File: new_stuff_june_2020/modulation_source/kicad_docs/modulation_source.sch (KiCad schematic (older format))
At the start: 72 parts, among them J1 power_in, Q1 BC560, Q2 BC560, Q3 BF245A, Q4 BC550, Q5 BC550, Q6 BC550, U1 LM13700, U2 TL072, U3 TL072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

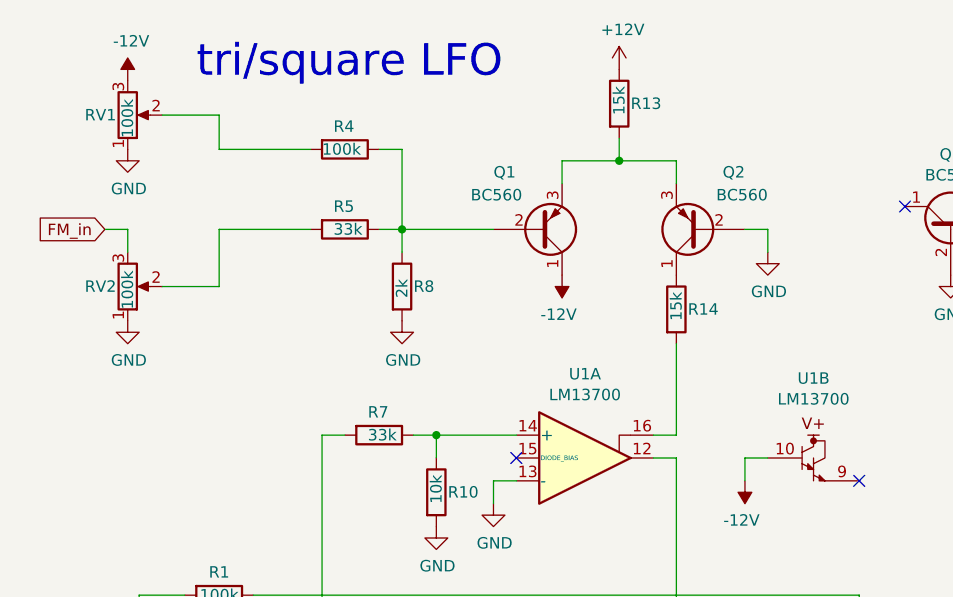
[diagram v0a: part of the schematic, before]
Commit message: change modulation-source fm circuit, make new gerbers
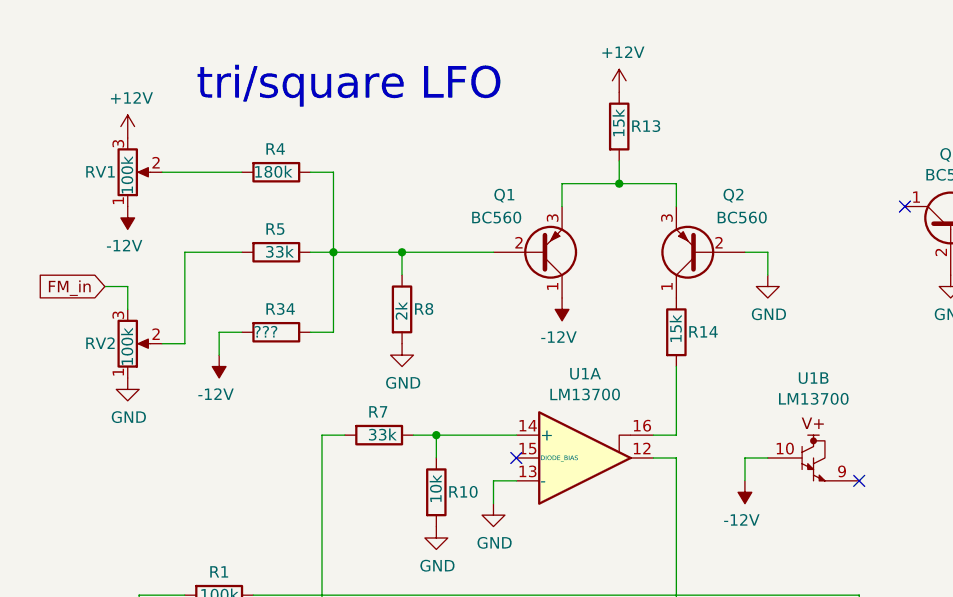
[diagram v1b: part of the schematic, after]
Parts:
- added R34: ???, Resistor_SMD:R_0805_2012Metric_Pad1.15x1.40mm_HandSolder, symbol Device:R
- R4: value 100k -> 180k
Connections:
- net +12V: now also RV1.3
- net -12V: now also RV1.1, R34.2; no longer RV1.3
- net GND: no longer RV1.1
- net at Q1.2 (B), R4.1, R5.1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: now also R34.1
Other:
- moved on the sheet: Q1, Q2, R13, R14, R4, R5, R8, RV1, RV2

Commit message: add some missing resistor values
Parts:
- R6, R9: value ??? -> 2k
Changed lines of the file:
@@
 P 2000 3750
 F 0 "R6" V 1900 3700 50  0000 L CNN
-F 1 "???" V 2000 3700 50  0000 L CNN
+F 1 "2k" V 2000 3700 50  0000 L CNN
 F 2 "Resistor_SMD:R_0805_2012Metric_Pad1.15x1.40mm_HandSolder" V 1930 3750 50  0001 C CNN
 F 3 "~" H 2000 3750 50  0001 C CNN
@@
 P 2250 4000
 F 0 "R9" H 2300 4000 50  0000 L CNN
-F 1 "???" V 2250 3950 50  0000 L CNN
+F 1 "2k" V 2250 3950 50  0000 L CNN
 F 2 "Resistor_SMD:R_0805_2012Metric_Pad1.15x1.40mm_HandSolder" V 2180 4000 50  0001 C CNN
 F 3 "~" H 2250 4000 50  0001 C CNN

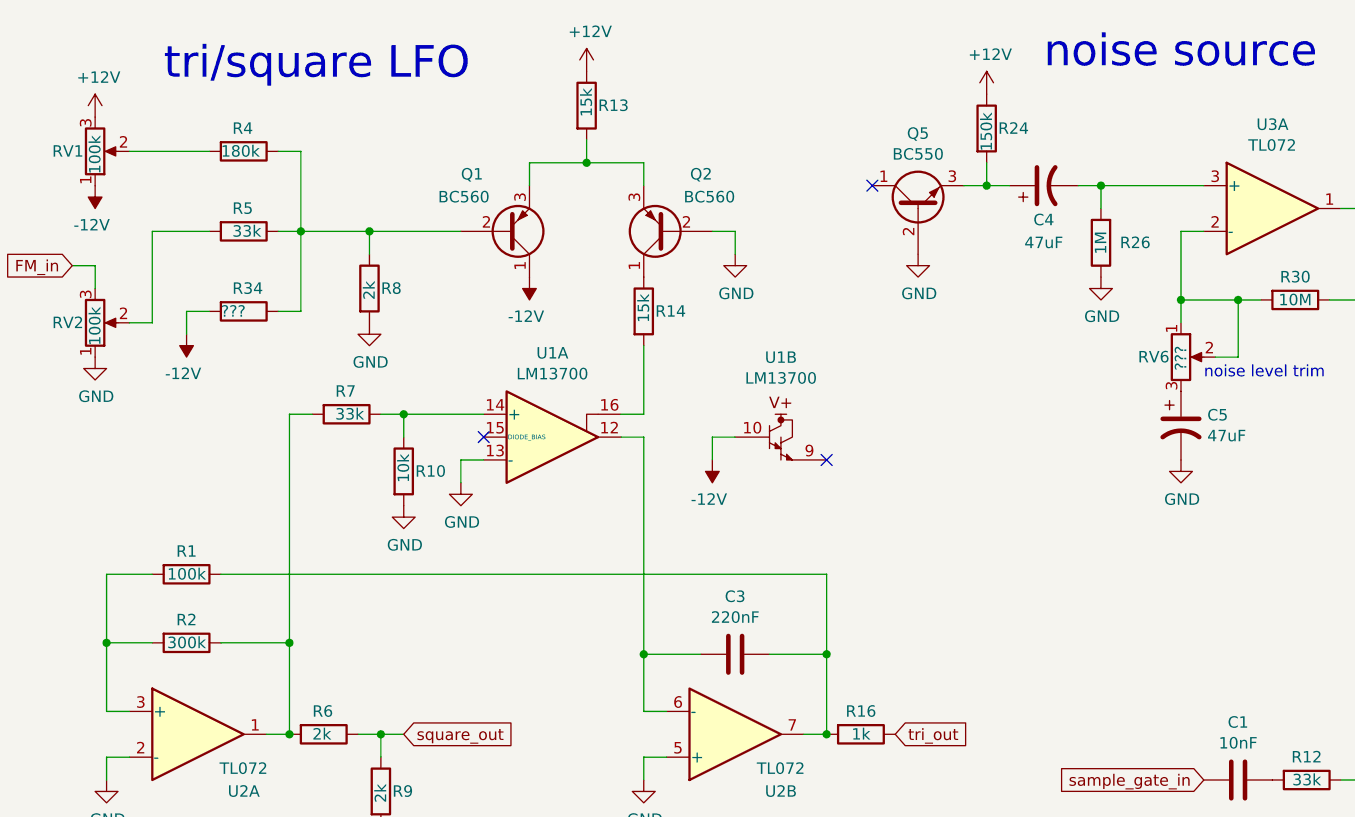
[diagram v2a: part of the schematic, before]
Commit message: update values to scale frequency and noise level
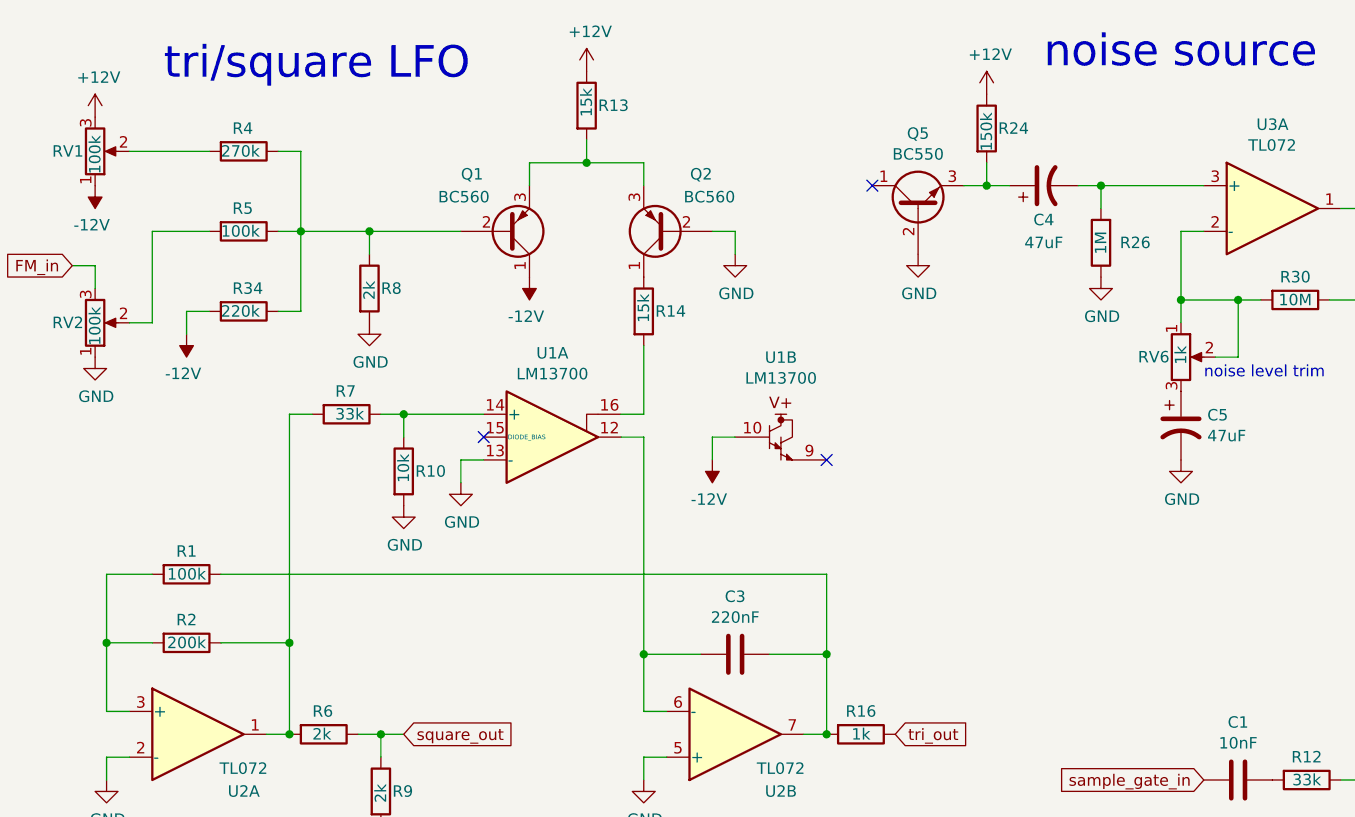
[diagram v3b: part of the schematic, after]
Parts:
- R2: value 300k -> 200k
- R34: value ??? -> 220k
- R4: value 180k -> 270k
- R5: value 33k -> 100k
- RV6: value ??? -> 1k
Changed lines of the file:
@@
-$EndComp
-$Comp
-L Device:R R5
-U 1 1 5EEF5608
-P 1650 1550
-F 0 "R5" V 1550 1500 50  0000 L CNN
-F 1 "33k" V 1650 1500 50  0000 L CNN
-F 2 "Resistor_SMD:R_0805_2012Metric_Pad1.15x1.40mm_HandSolder" V 1580 1550 50  0001 C CNN
-F 3 "~" H 1650 1550 50  0001 C CNN
-	1    1650 1550
-	0    1    1    0
-$EndComp
-$Comp
-L Device:R R8
-U 1 1 5EEF5DDB
-P 2200 1800
-F 0 "R8" H 2250 1800 50  0000 L CNN
-F 1 "2k" V 2200 1750 50  0000 L CNN
-F 2 "Resistor_SMD:R_0805_2012Metric_Pad1.15x1.40mm_HandSolder" V 2130 1800 50  0001 C CNN
-F 3 "~" H 2200 1800 50  0001 C CNN
-	1    2200 1800
-	1    0    0    -1
 $EndComp
 $Comp
@@
 	1    0    0    -1
 $EndComp
-$Comp
-L Device:R R4
-U 1 1 5EEF67D4
-P 1650 1200
-F 0 "R4" V 1550 1150 50  0000 L CNN
-F 1 "180k" V 1650 1100 50  0000 L CNN
-F 2 "Resistor_SMD:R_0805_2012Metric_Pad1.15x1.40mm_HandSolder" V 1580 1200 50  0001 C CNN
-F 3 "~" H 1650 1200 50  0001 C CNN
-	1    1650 1200
-	0    1    1    0
-$EndComp
 Wire Wire Line
 	1800 1550 1900 1550
@@
 P 1400 3350
 F 0 "R2" V 1300 3350 50  0000 C CNN
-F 1 "300k" V 1400 3350 50  0000 C CNN
+F 1 "200k" V 1400 3350 50  0000 C CNN
 F 2 "Resistor_SMD:R_0805_2012Metric_Pad1.15x1.40mm_HandSolder" V 1330 3350 50  0001 C CNN
 F 3 "~" H 1400 3350 50  0001 C CNN
@@
 P 5750 2100
 F 0 "RV6" H 5700 2100 50  0000 R CNN
-F 1 "???" V 5750 2150 50  0000 R CNN
+F 1 "1k" V 5750 2150 50  0000 R CNN
 F 2 "Potentiometer_THT:Potentiometer_Bourns_3296W_Vertical" H 5750 2100 50  0001 C CNN
 F 3 "~" H 5750 2100 50  0001 C CNN
@@
 Wire Wire Line
 	3400 2350 3400 2050
-$Comp
-L Device:R R34
-U 1 1 5EF5CFC9
-P 1650 1900
-F 0 "R34" V 1550 1850 50  0000 L CNN
-F 1 "???" V 1650 1800 50  0000 L CNN
-F 2 "Resistor_SMD:R_0805_2012Metric_Pad1.15x1.40mm_HandSolder" V 1580 1900 50  0001 C CNN
-F 3 "~" H 1650 1900 50  0001 C CNN
-	1    1650 1900
-	0    1    1    0
-$EndComp
 Wire Wire Line
 	1800 1900 1900 1900
@@
 Wire Wire Line
 	1400 1900 1500 1900
+$Comp
+L Device:R R5
+U 1 1 5EEF5608
+P 1650 1550
+F 0 "R5" V 1550 1500 50  0000 L CNN
+F 1 "100k" V 1650 1450 50  0000 L CNN
+F 2 "Resistor_SMD:R_0805_2012Metric_Pad1.15x1.40mm_HandSolder" V 1580 1550 50  0001 C CNN
+F 3 "~" H 1650 1550 50  0001 C CNN
+	1    1650 1550
+	0    1    1    0
+$EndComp
+$Comp
+L Device:R R34
+U 1 1 5EF5CFC9
+P 1650 1900
+F 0 "R34" V 1550 1850 50  0000 L CNN
+F 1 "220k" V 1650 1800 50  0000 L CNN
+F 2 "Resistor_SMD:R_0805_2012Metric_Pad1.15x1.40mm_HandSolder" V 1580 1900 50  0001 C CNN
+F 3 "~" H 1650 1900 50  0001 C CNN
+	1    1650 1900
+	0    1    1    0
+$EndComp
+$Comp
+L Device:R R8
+U 1 1 5EEF5DDB
+P 2200 1800
+F 0 "R8" H 2250 1800 50  0000 L CNN
+F 1 "2k" V 2200 1750 50  0000 L CNN
+F 2 "Resistor_SMD:R_0805_2012Metric_Pad1.15x1.40mm_HandSolder" V 2130 1800 50  0001 C CNN
+F 3 "~" H 2200 1800 50  0001 C CNN
+	1    2200 1800
+	1    0    0    -1
+$EndComp
+$Comp
+L Device:R R4
+U 1 1 5EEF67D4
+P 1650 1200
+F 0 "R4" V 1550 1150 50  0000 L CNN
+F 1 "270k" V 1650 1100 50  0000 L CNN
+F 2 "Resistor_SMD:R_0805_2012Metric_Pad1.15x1.40mm_HandSolder" V 1580 1200 50  0001 C CNN
+F 3 "~" H 1650 1200 50  0001 C CNN
+	1    1650 1200
+	0    1    1    0
+$EndComp
 $EndSCHEMATC
